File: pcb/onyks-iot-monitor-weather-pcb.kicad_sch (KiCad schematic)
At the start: 0 parts

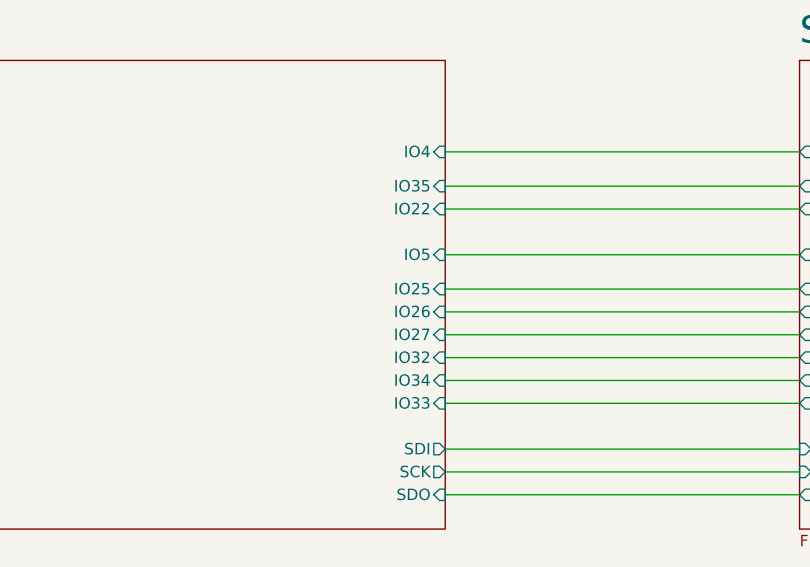
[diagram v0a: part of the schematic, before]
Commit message: PCB jeszcze mniejsza wersja
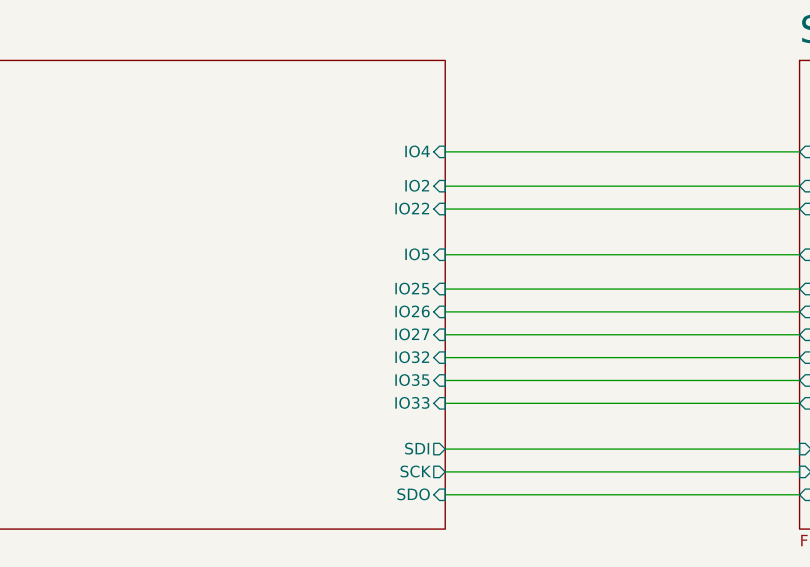
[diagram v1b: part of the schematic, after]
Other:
- sheet ESP32 ports: added IO2; removed IO34
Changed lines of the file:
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@@
 			)
 		)
-		(pin "IO34" input
-			(at 135.89 104.14 0)
+		(pin "IO2" input
+			(at 135.89 82.55 0)
 			(effects
 				(font
@@
 		)
 		(pin "IO35" input
-			(at 135.89 82.55 0)
+			(at 135.89 104.14 0)
 			(effects
 				(font

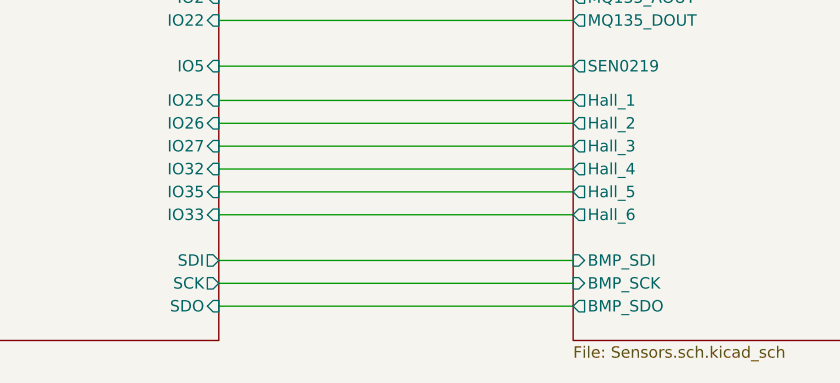
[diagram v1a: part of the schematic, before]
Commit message: 4 layer PCB
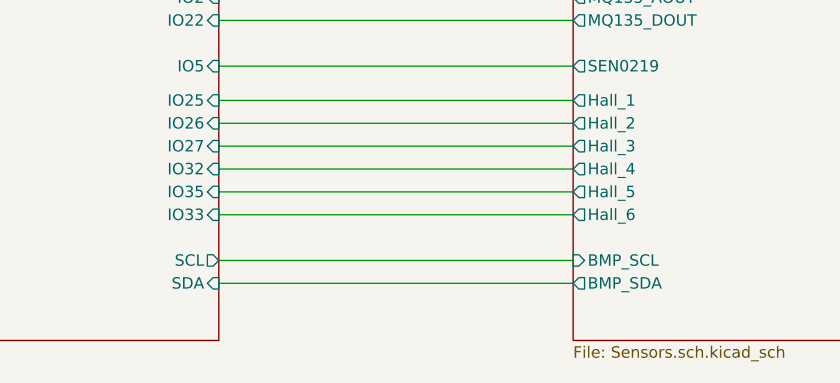
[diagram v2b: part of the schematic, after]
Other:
- sheet ESP32 ports: added SCL, SDA; removed SCK, SDI, SDO
- sheet Sensors ports: added BMP_SCL, BMP_SDA; removed BMP_SCK, BMP_SDI, BMP_SDO
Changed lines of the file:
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@@
-	(wire
-		(pts
-			(xy 135.89 116.84) (xy 175.26 116.84)
-		)
-		(stroke
-			(width 0)
-			(type default)
-		)
-	)
 	(wire
 		(pts
@@
 			)
 		)
-		(pin "SCK" output
-			(at 135.89 114.3 0)
-			(effects
-				(font
-					(size 1.27 1.27)
-				)
-				(justify right)
-			)
-		)
-		(pin "SDI" output
-			(at 135.89 111.76 0)
-			(effects
-				(font
-					(size 1.27 1.27)
-				)
-				(justify right)
-			)
-		)
 		(pin "IO32" input
 			(at 135.89 101.6 0)
@@
 			)
 		)
-		(pin "SDO" input
-			(at 135.89 116.84 0)
-			(effects
-				(font
-					(size 1.27 1.27)
-				)
-				(justify right)
-			)
-		)
 		(pin "IO33" input
 			(at 135.89 106.68 0)
@@
 		(pin "IO35" input
 			(at 135.89 104.14 0)
+			(effects
+				(font
+					(size 1.27 1.27)
+				)
+				(justify right)
+			)
+		)
+		(pin "SCL" output
+			(at 135.89 111.76 0)
+			(effects
+				(font
+					(size 1.27 1.27)
+				)
+				(justify right)
+			)
+		)
+		(pin "SDA" input
+			(at 135.89 114.3 0)
 			(effects
 				(font
@@
 			)
 		)
-		(pin "BMP_SDI" input
-			(at 175.26 111.76 180)
-			(effects
-				(font
-					(size 1.27 1.27)
-				)
-				(justify left)
-			)
-		)
-		(pin "BMP_SCK" input
-			(at 175.26 114.3 180)
-			(effects
-				(font
-					(size 1.27 1.27)
-				)
-				(justify left)
-			)
-		)
-		(pin "BMP_SDO" output
-			(at 175.26 116.84 180)
-			(effects
-				(font
-					(size 1.27 1.27)
-				)
-				(justify left)
-			)
-		)
 		(pin "Hall_3" output
 			(at 175.26 99.06 180)
@@
 			(effects
 				(font
+					(size 1.27 1.27)
+				)
+				(justify left)
+			)
+		)
+		(pin "BMP_SCL" input
+			(at 175.26 111.76 180)
+			(effects
+				(font
+					(size 1.27 1.27)
+				)
+				(justify left)
+			)
+		)
+		(pin "BMP_SDA" output
+			(at 175.26 114.3 180)
+			(effects
+				(font
